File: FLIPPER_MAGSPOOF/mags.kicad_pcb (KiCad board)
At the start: 2 copper layers, 66 x 30.5 mm, 25 parts, among them J1 Coil, J2 Conn_01x10_Socket, J3 Conn_01x08_Socket, J4 Conn_01x08_Socket, J5 Conn_01x10_Socket, U1 TC4424

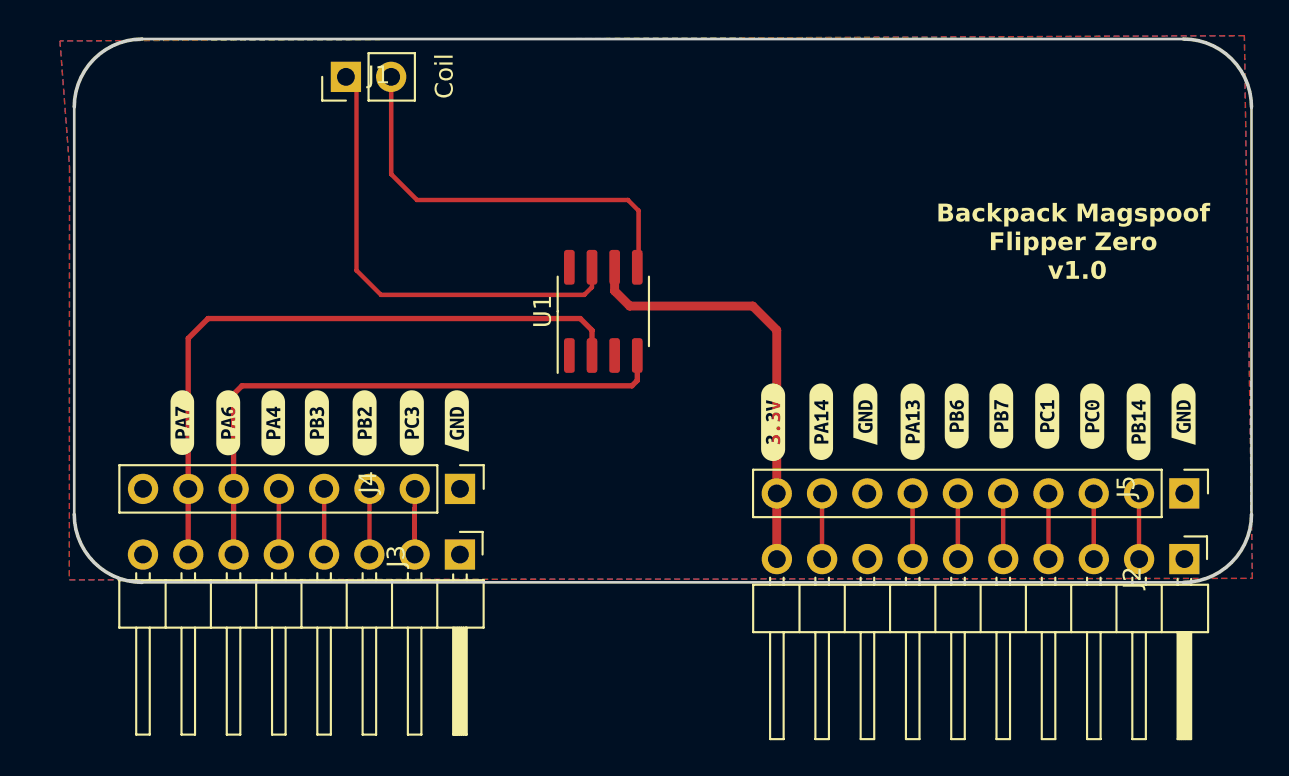
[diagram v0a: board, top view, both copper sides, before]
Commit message: Add_SW_3/5v
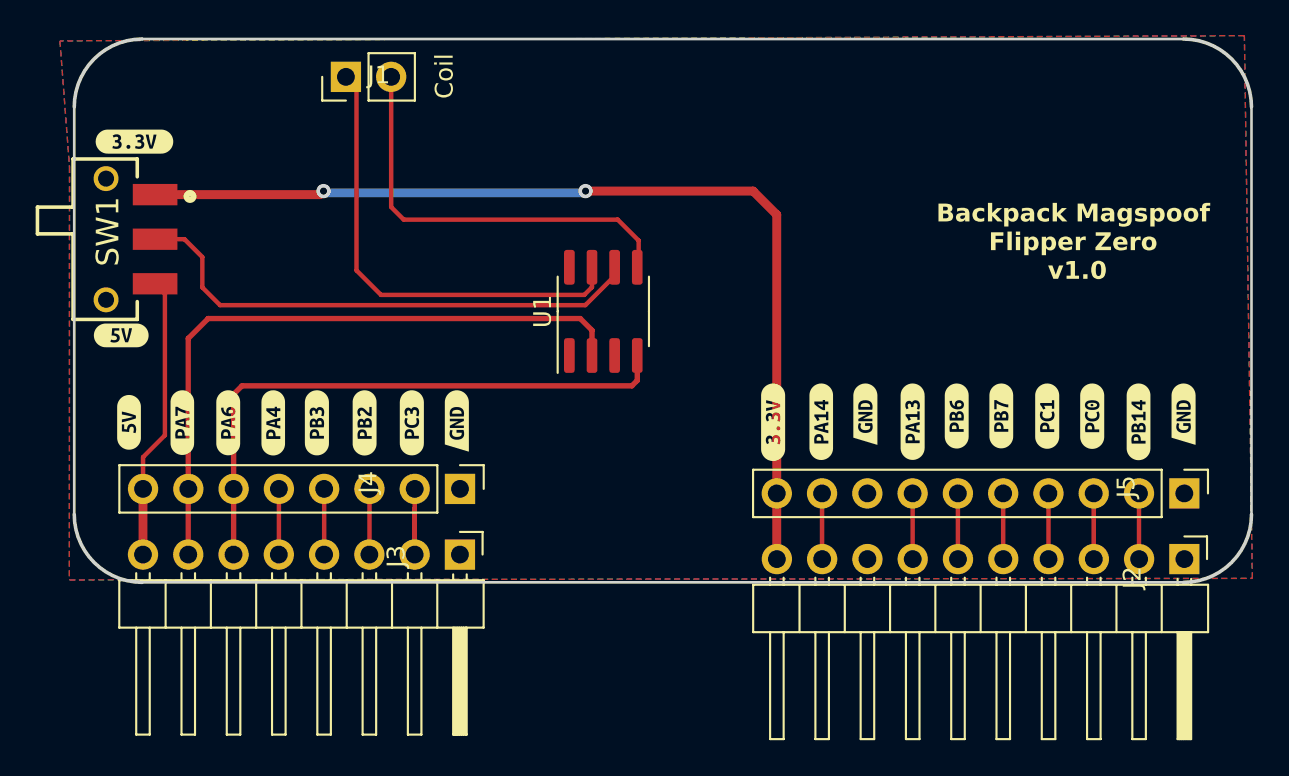
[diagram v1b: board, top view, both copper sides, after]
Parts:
- added SW1: On, footprintsg:JS102011SAQN, F.Cu at (199.8, 67.4)
- added kibuzzard-6488F75A: G***, kibuzzard-6488F75A, F.Cu at (199.6, 61.9)
- added kibuzzard-649DB344: G***, kibuzzard-649DB344, F.Cu at (198.9, 72.8)
- added kibuzzard-649DB344: G***, kibuzzard-649DB344, F.Cu at (199.3, 77.7)
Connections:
- J3 pad 8: unconnected-(J3-Pin_1-Pad8) -> +5V
- J4 pad 8: unconnected-(J4-Pin_1-Pad8) -> +5V
- U1 pad 6: +3V3 -> /VDD
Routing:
- net +3V3: track 24.2 -> 54.9 mm, vias 0 -> 2
- net /VDD: track 0.00 -> 29.5 mm
- net +5V: track 0.00 -> 15.9 mm
